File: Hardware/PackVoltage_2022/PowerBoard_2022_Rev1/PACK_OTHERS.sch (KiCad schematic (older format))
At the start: 50 parts

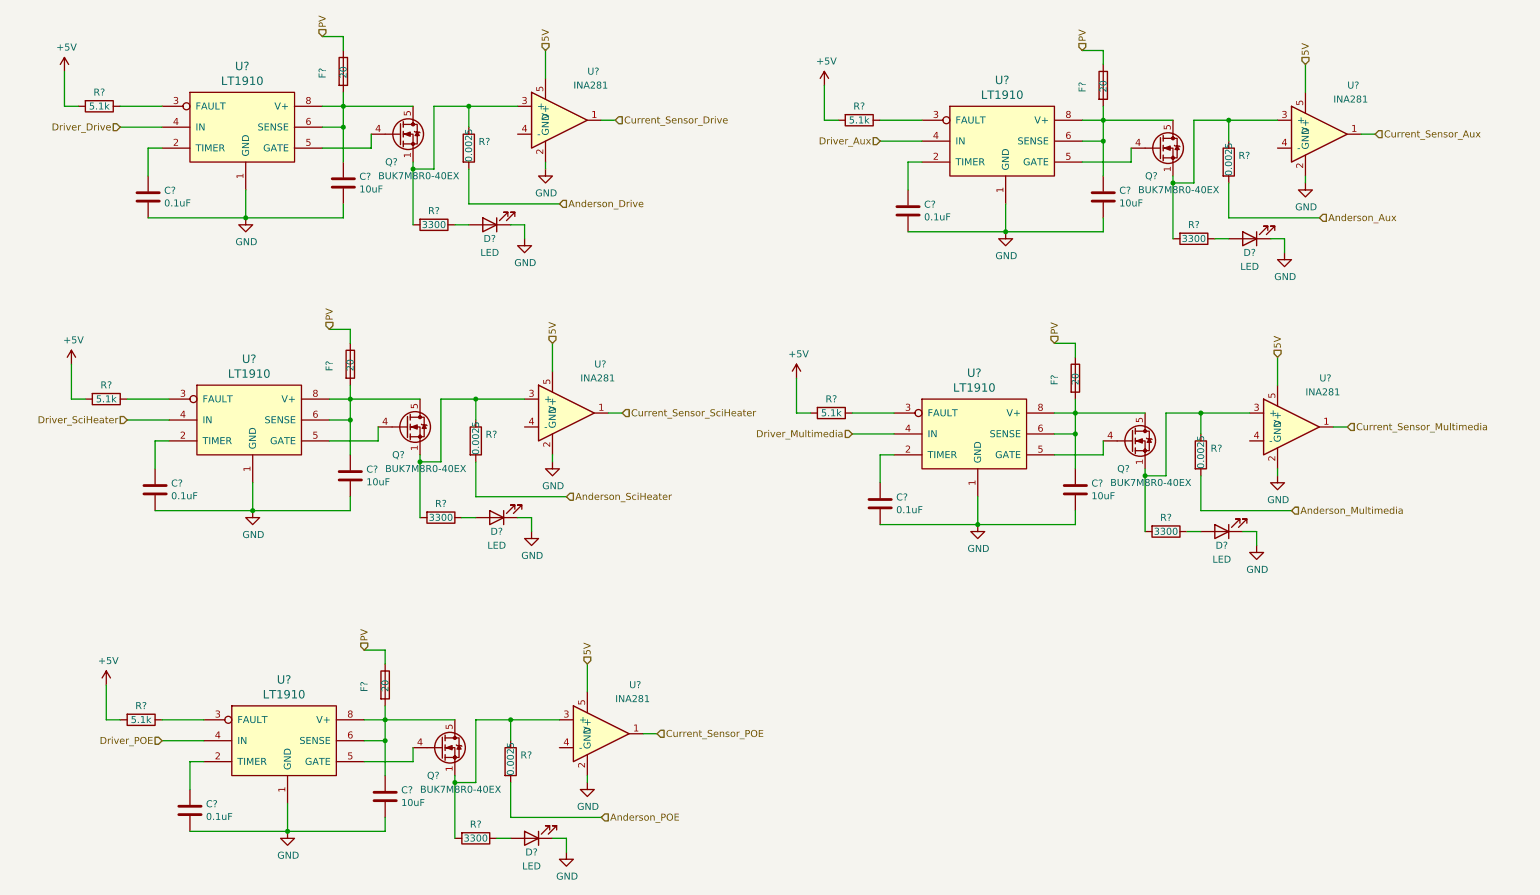
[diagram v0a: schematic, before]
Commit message: TIVA and fixed 12V
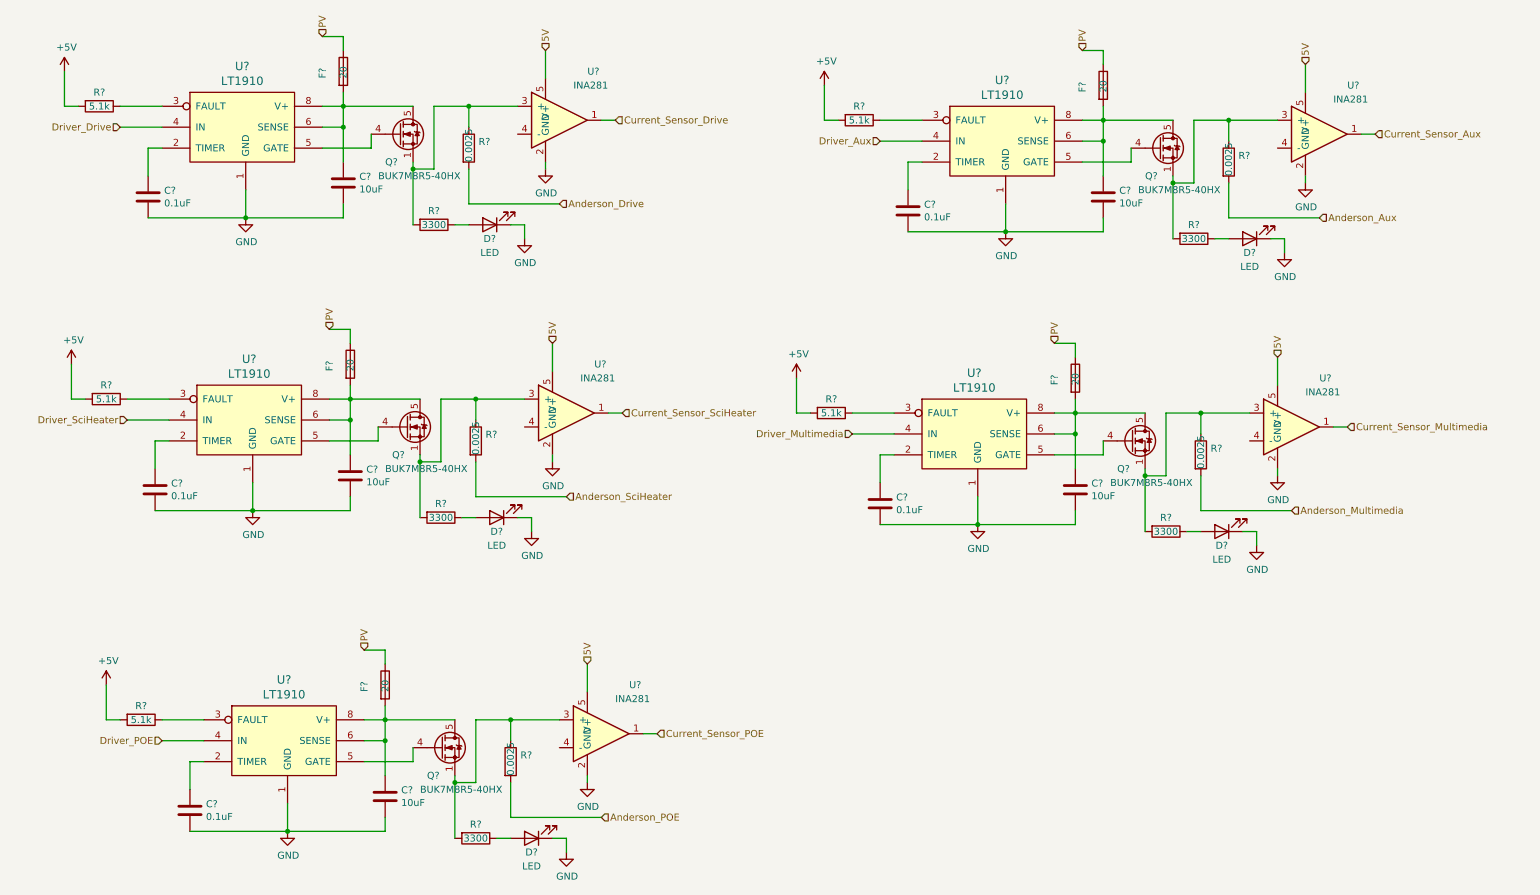
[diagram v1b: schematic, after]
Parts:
- Q? (x5): value BUK7M8R0-40EX -> BUK7M8R5-40HX
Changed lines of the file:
@@
 $Descr A4 11693 8268
 encoding utf-8
-Sheet 10 10
+Sheet 6 9
 Title ""
 Date ""
@@
 AR Path="/61609A41/6160E165" Ref="Q?"  Part="1"
 F 0 "Q?" H 3100 1600 50  0000 L CNN
-F 1 "BUK7M8R0-40EX" H 3050 1500 50  0000 L CNN
+F 1 "BUK7M8R5-40HX" H 3050 1500 50  0000 L CNN
 F 2 "Package_TO_SOT_SMD:LFPAK33" H 3400 1725 50  0001 L CIN
 F 3 "https://assets.nexperia.com/documents/data-sheet/BUK7M8R0-40E.pdf" V 3200 1800 50  0001 L CNN
@@
 Wire Wire Line
 	8250 1200 8250 1300
-$Comp
-L Transistor_FET:BUK7M8R0-40EX Q?
-U 1 1 61612B40
-P 8650 1900
-AR Path="/615D5992/61612B40" Ref="Q?"  Part="1"
-AR Path="/61609A41/61612B40" Ref="Q?"  Part="1"
-F 0 "Q?" H 8550 1700 50  0000 L CNN
-F 1 "BUK7M8R0-40EX" H 8500 1600 50  0000 L CNN
-F 2 "Package_TO_SOT_SMD:LFPAK33" H 8850 1825 50  0001 L CIN
-F 3 "https://assets.nexperia.com/documents/data-sheet/BUK7M8R0-40E.pdf" V 8650 1900 50  0001 L CNN
-	1    8650 1900
-	1    0    0    -1
-$EndComp
 Wire Wire Line
 	8250 1700 8750 1700
@@
 AR Path="/61609A41/6161A090" Ref="Q?"  Part="1"
 F 0 "Q?" H 3150 3700 50  0000 L CNN
-F 1 "BUK7M8R0-40EX" H 3100 3600 50  0000 L CNN
+F 1 "BUK7M8R5-40HX" H 3100 3600 50  0000 L CNN
 F 2 "Package_TO_SOT_SMD:LFPAK33" H 3450 3825 50  0001 L CIN
 F 3 "https://assets.nexperia.com/documents/data-sheet/BUK7M8R0-40E.pdf" V 3250 3900 50  0001 L CNN
@@
 AR Path="/61609A41/616211F5" Ref="Q?"  Part="1"
 F 0 "Q?" H 8350 3800 50  0000 L CNN
-F 1 "BUK7M8R0-40EX" H 8300 3700 50  0000 L CNN
+F 1 "BUK7M8R5-40HX" H 8300 3700 50  0000 L CNN
 F 2 "Package_TO_SOT_SMD:LFPAK33" H 8650 3925 50  0001 L CIN
 F 3 "https://assets.nexperia.com/documents/data-sheet/BUK7M8R0-40E.pdf" V 8450 4000 50  0001 L CNN
@@
 AR Path="/61609A41/616288D7" Ref="Q?"  Part="1"
 F 0 "Q?" H 3400 6000 50  0000 L CNN
-F 1 "BUK7M8R0-40EX" H 3350 5900 50  0000 L CNN
+F 1 "BUK7M8R5-40HX" H 3350 5900 50  0000 L CNN
 F 2 "Package_TO_SOT_SMD:LFPAK33" H 3700 6125 50  0001 L CIN
 F 3 "https://assets.nexperia.com/documents/data-sheet/BUK7M8R0-40E.pdf" V 3500 6200 50  0001 L CNN
@@
 	3750 6000 4000 6000
 Connection ~ 4000 6000
+$Comp
+L Transistor_FET:BUK7M8R0-40EX Q?
+U 1 1 61612B40
+P 8650 1900
+AR Path="/615D5992/61612B40" Ref="Q?"  Part="1"
+AR Path="/61609A41/61612B40" Ref="Q?"  Part="1"
+F 0 "Q?" H 8550 1700 50  0000 L CNN
+F 1 "BUK7M8R5-40HX" H 8500 1600 50  0000 L CNN
+F 2 "Package_TO_SOT_SMD:LFPAK33" H 8850 1825 50  0001 L CIN
+F 3 "https://assets.nexperia.com/documents/data-sheet/BUK7M8R0-40E.pdf" V 8650 1900 50  0001 L CNN
+	1    8650 1900
+	1    0    0    -1
+$EndComp
 $EndSCHEMATC

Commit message: Fixed some stuff
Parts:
- removed C? (x2): 0.1uF, symbol Device:C
- removed C? (x2): 10uF, symbol Device:C
- removed D? (x2): LED, symbol Device:LED
- removed F? (x2): 20, symbol Device:Fuse
- removed Q? (x2): BUK7M8R5-40HX, Package_TO_SOT_SMD:LFPAK33, symbol Transistor_FET:BUK7M8R0-40EX
- removed R? (x2): 5.1k, symbol Device:R
- removed R? (x2): 3300, symbol Device:R
- removed R? (x2): 0.0025, symbol Device:R
- removed U? (x2): LT1910, symbol PowerBoard_2022_Rev1-rescue:LT1910-MRDT_ICs
- removed U? (x2): INA281, Package_TO_SOT_SMD:SOT-23-5, symbol PowerBoard_2022_Rev1-rescue:INA281-MRDT_ICs
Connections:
- net Anderson_Aux: now also U?.4 (-)
- net Anderson_POE: now also U?.4 (-)
- net Anderson_SciHeater: now also U?.4 (-)

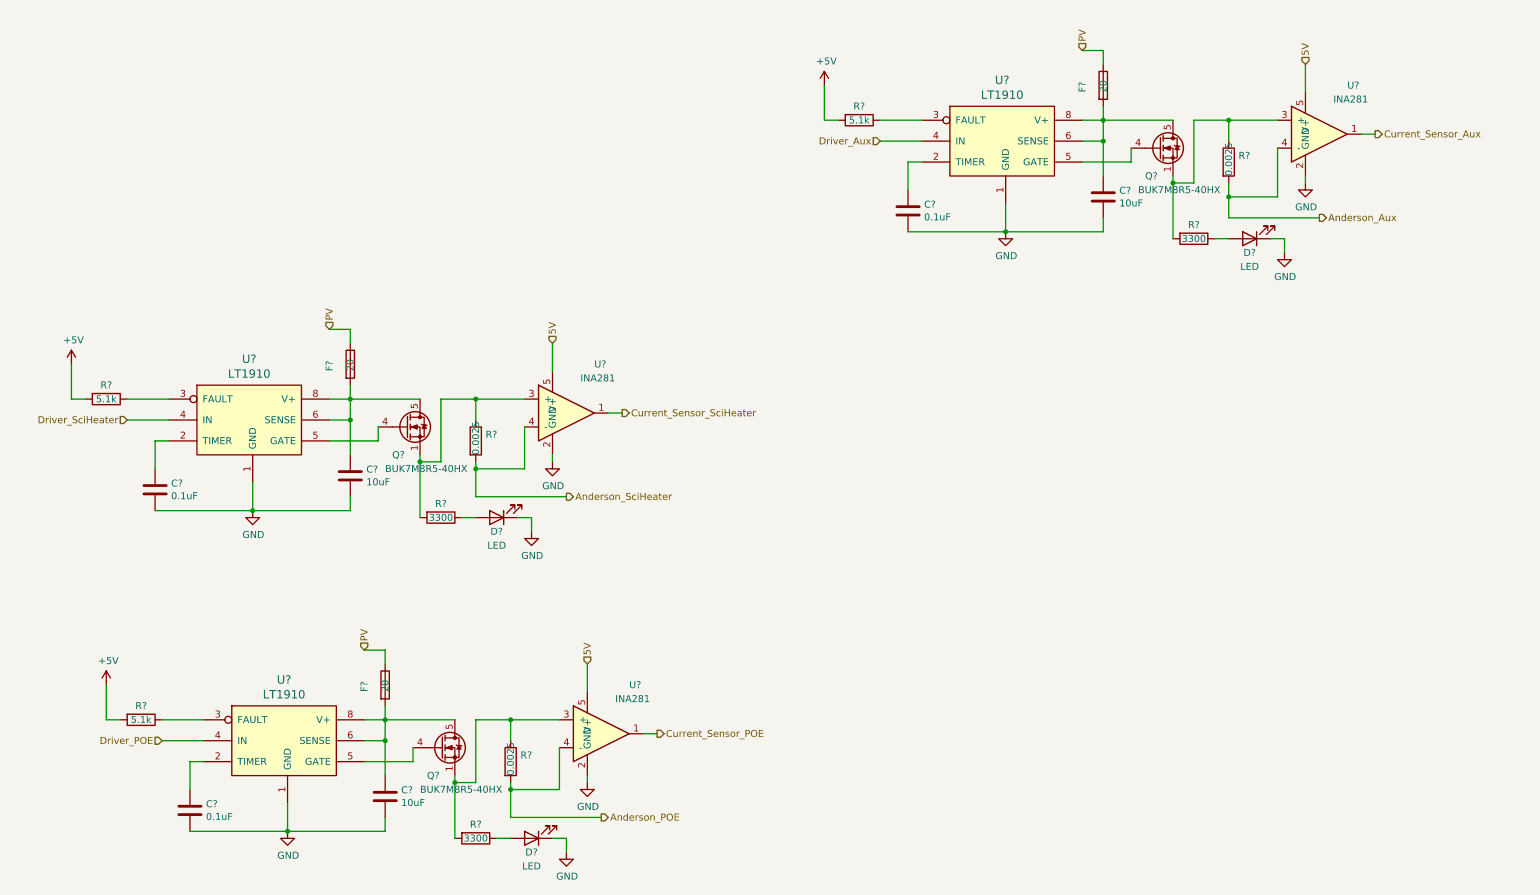
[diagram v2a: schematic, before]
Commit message: Changed values of LED resistors, changed some of the outputs to inputs, and made board look better
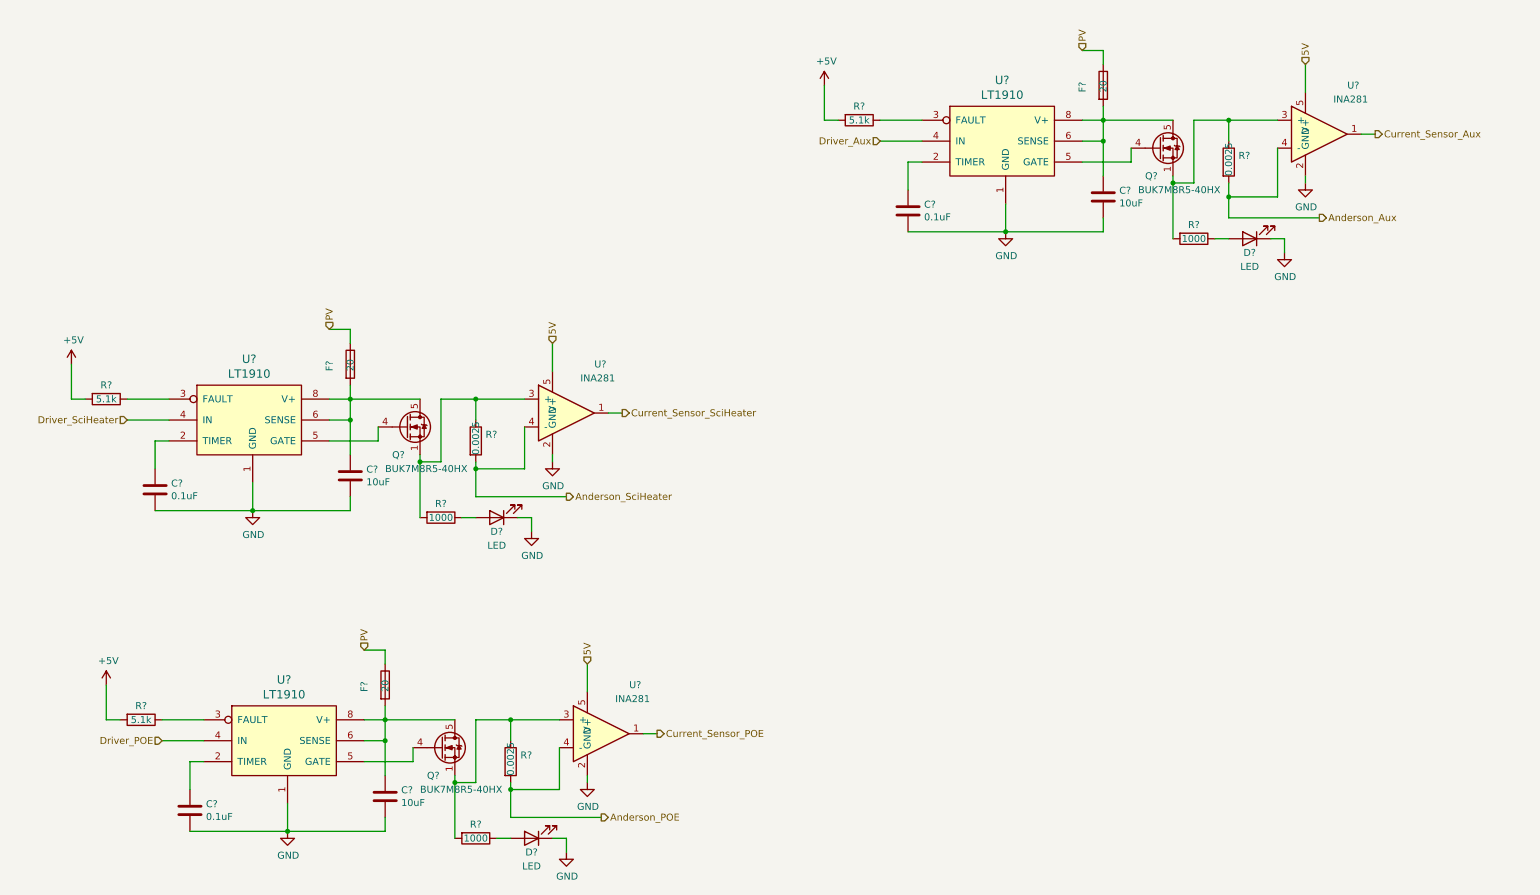
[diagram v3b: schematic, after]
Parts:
- R? (x3): value 3300 -> 1000
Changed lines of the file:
@@
 $Descr A4 11693 8268
 encoding utf-8
-Sheet 4 9
+Sheet 3 9
 Title ""
 Date ""
@@
 AR Path="/61609A41/61612B53" Ref="R?"  Part="1"
 F 0 "R?" V 8800 2550 50  0000 C CNN
-F 1 "3300" V 8900 2550 50  0000 C CNN
+F 1 "1000" V 8900 2550 50  0000 C CNN
 F 2 "" V 8830 2550 50  0001 C CNN
 F 3 "~" H 8900 2550 50  0001 C CNN
@@
 AR Path="/61609A41/6161A0A3" Ref="R?"  Part="1"
 F 0 "R?" V 3400 4550 50  0000 C CNN
-F 1 "3300" V 3500 4550 50  0000 C CNN
+F 1 "1000" V 3500 4550 50  0000 C CNN
 F 2 "" V 3430 4550 50  0001 C CNN
 F 3 "~" H 3500 4550 50  0001 C CNN
@@
 AR Path="/61609A41/616288EA" Ref="R?"  Part="1"
 F 0 "R?" V 3650 6850 50  0000 C CNN
-F 1 "3300" V 3750 6850 50  0000 C CNN
+F 1 "1000" V 3750 6850 50  0000 C CNN
 F 2 "" V 3680 6850 50  0001 C CNN
 F 3 "~" H 3750 6850 50  0001 C CNN

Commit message: Minor changes with Powerboard PDF
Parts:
- gave numbers to parts that had none: 30
